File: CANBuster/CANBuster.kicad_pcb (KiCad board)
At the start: 2 copper layers, 100 x 100 mm, 182 parts, among them CON1 BARREL_JACK, J1 RJ45, J2 RJ45, J3 RJ12, P1 CONN_01X10, P10 CONN_02X04, P11 RS232-Programmer, P12 S88, P13 CONN_01X10, P14 CONN_01X10, P15 TRACK, P16 CONN_01X02, P17 USB_OTG, P18 CONN_01X04, P2 CONN_01X10, P3 CONN_01X03, P4 CONN_01X03, P5 CONN_01X03, P6 CONN_01X03, P7 CONN_01X02, P8 CONN_01X06, P9 CONN_01X04, Q1 BC547, Q2 BC547, SW1 SW_PUSH, SW2 SW_PUSH, U1 PIC18F45K80, U12 MCP2561, U2 MCP2561, U3 7805, U4 LTV-844, U5 LTV-844, U6 LTV-844, U7 LTV-844, U8 ISO1050, Y1 16MHz

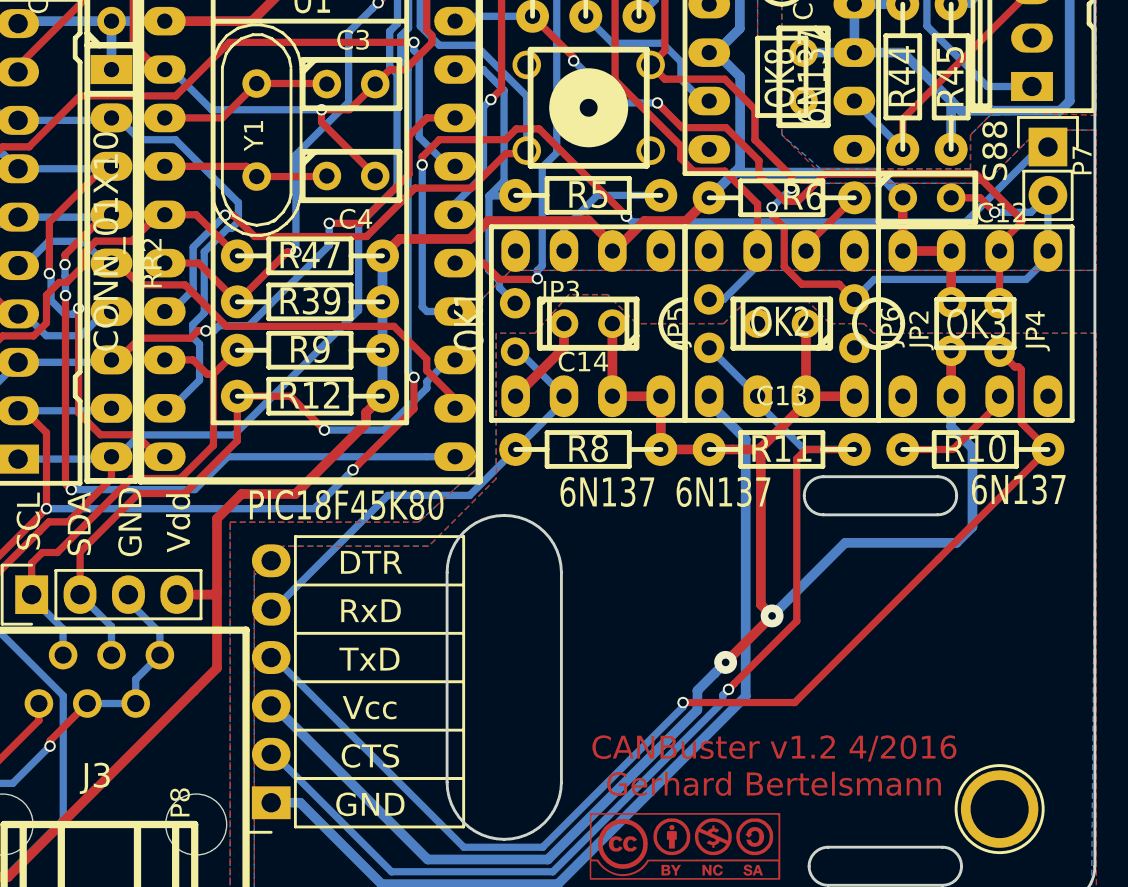
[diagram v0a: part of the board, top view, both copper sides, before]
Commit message: PCB: fix CCP2 pin
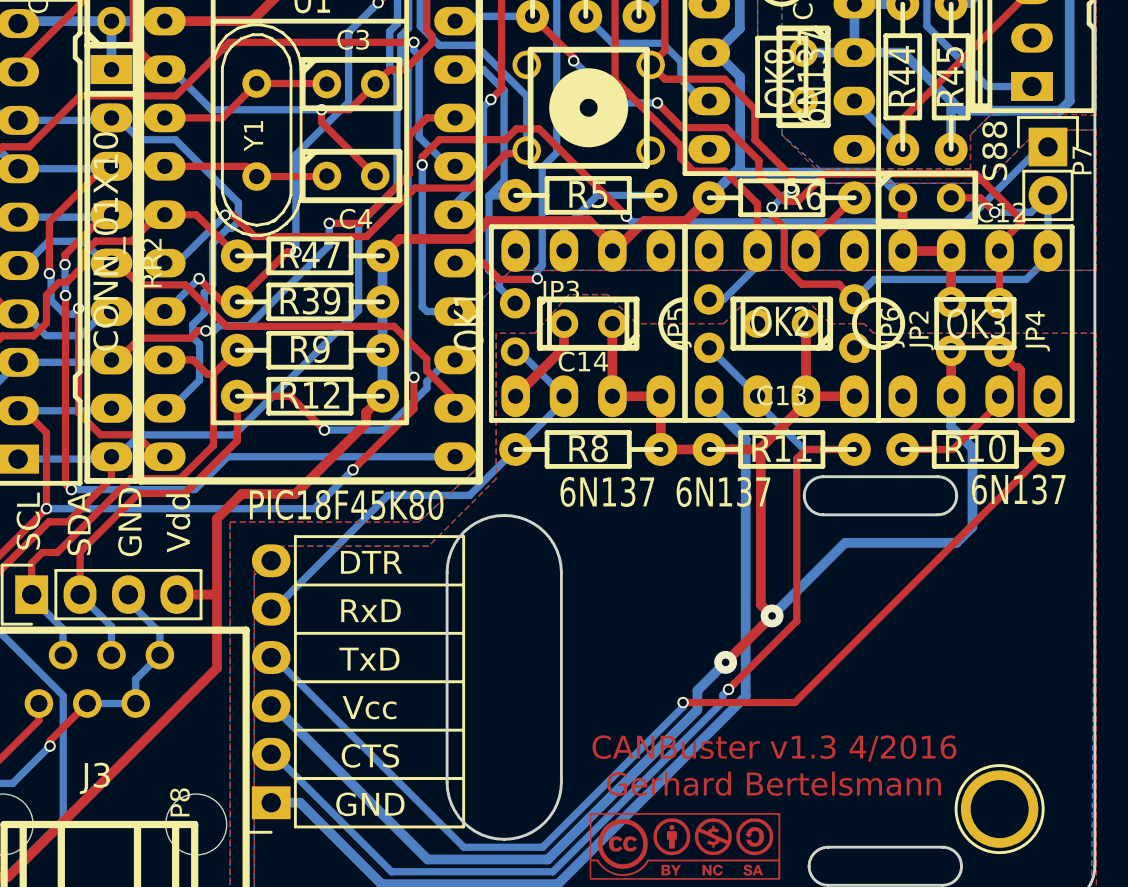
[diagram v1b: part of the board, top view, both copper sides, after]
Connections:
- U1 pad 16: /PWM1 -> /STATUS
- U1 pad 17: /STATUS -> /PWM1
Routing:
- net /STATUS: track 95.6 -> 93.3 mm
- net /PWM1: track 68.0 -> 68.4 mm, vias 2 -> 3
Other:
- board text added: "CANBuster v1.3 4/2016 Gerhard Bertelsmann"
- board text removed: "CANBuster v1.2 4/2016 Gerhard Bertelsmann"
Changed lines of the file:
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@@
-(kicad_pcb (version 4) (host pcbnew 4.0.1-stable)
+(kicad_pcb (version 4) (host pcbnew 4.0.2-4+6225~38~ubuntu14.04.1-stable)
   (general
     (links 464)
     (no_connects 0)
-    (area 70.028999 35.052999 170.179001 135.203001)
+    (area 69.215499 29.4545 181.99 144.85554)
     (thickness 1.6)
     (drawings 39)
-    (tracks 1769)
+    (tracks 1776)
     (zones 0)
     (modules 182)
@@
       (net 77 /SNIFF))
     (pad 16 thru_hole oval (at 13.97 7.62 270) (size 1.50114 2.19964) (drill 0.8001) (layers *.Cu *.Mask F.SilkS)
-      (net 26 /PWM1))
-    (pad 17 thru_hole oval (at 16.51 7.62 270) (size 1.50114 2.19964) (drill 0.8001) (layers *.Cu *.Mask F.SilkS)
       (net 59 /STATUS))
+    (pad 17 thru_hole oval (at 16.51 7.62 270) (size 1.50114 2.19964) (drill 0.8001) (layers *.Cu *.Mask F.SilkS)
+      (net 26 /PWM1))
     (pad 18 thru_hole oval (at 19.05 7.62 270) (size 1.50114 2.19964) (drill 0.8001) (layers *.Cu *.Mask F.SilkS)
       (net 30 /SCL))
@@
     (effects (font (size 1.2 1.2) (thickness 0.2)))
   )
-  (gr_text "CANBuster v1.2 4/2016\nGerhard Bertelsmann" (at 153.289 127.889) (layer F.Cu)
+  (gr_text "CANBuster v1.3 4/2016\nGerhard Bertelsmann" (at 153.289 127.889) (layer F.Cu)
     (effects (font (size 1.2 1.2) (thickness 0.25)))
   )
@@
   (segment (start 112.2172 86.233) (end 113.5888 86.233) (width 0.381) (layer B.Cu) (net 17))
   (segment (start 111.5822 85.598) (end 112.2172 86.233) (width 0.381) (layer B.Cu) (net 17))
-  (segment (start 121.63425 109.093) (end 121.285 109.093) (width 0.381) (layer B.Cu) (net 18))
-  (segment (start 125.150502 99.289842) (end 124.791442 99.648902) (width 0.381) (layer B.Cu) (net 18))
-  (segment (start 124.791442 99.648902) (end 124.59117 99.648902) (width 0.381) (layer B.Cu) (net 18))
-  (segment (start 124.59117 99.648902) (end 123.356341 100.883731) (width 0.381) (layer B.Cu) (net 18))
+  (segment (start 123.356341 103.008459) (end 123.407141 103.008459) (width 0.381) (layer B.Cu) (net 18))
   (segment (start 122.753498 105.360442) (end 123.112558 105.719502) (width 0.381) (layer B.Cu) (net 18))
   (segment (start 123.112558 105.719502) (end 123.112558 107.614692) (width 0.381) (layer B.Cu) (net 18))
-  (segment (start 123.356341 100.883731) (end 123.356341 104.094715) (width 0.381) (layer B.Cu) (net 18))
   (segment (start 123.356341 104.094715) (end 122.753498 104.697558) (width 0.381) (layer B.Cu) (net 18))
   (segment (start 122.753498 104.697558) (end 122.753498 105.360442) (width 0.381) (layer B.Cu) (net 18))
-  (segment (start 118.491 93.853) (end 118.82882 93.853) (width 0.381) (layer B.Cu) (net 18))
-  (segment (start 118.82882 93.853) (end 119.97182 94.996) (width 0.381) (layer B.Cu) (net 18))
+  (segment (start 121.63425 109.093) (end 123.112558 107.614692) (width 0.381) (layer B.Cu) (net 18))
+  (segment (start 123.356341 104.094715) (end 123.356341 103.008459) (width 0.381) (layer B.Cu) (net 18))
+  (segment (start 124.591164 99.648896) (end 124.591164 99.648902) (width 0.381) (layer B.Cu) (net 18))
+  (segment (start 123.7996 100.44046) (end 124.591164 99.648896) (width 0.381) (layer B.Cu) (net 18))
+  (segment (start 123.7996 102.616) (end 123.7996 100.44046) (width 0.381) (layer B.Cu) (net 18))
+  (segment (start 123.407141 103.008459) (end 123.7996 102.616) (width 0.381) (layer B.Cu) (net 18))
+  (segment (start 125.150502 98.295522) (end 125.150502 99.289842) (width 0.381) (layer B.Cu) (net 18))
+  (segment (start 125.150502 99.289842) (end 124.791442 99.648902) (width 0.381) (layer B.Cu) (net 18))
+  (segment (start 124.791442 99.648902) (end 124.591164 99.648902) (width 0.381) (layer B.Cu) (net 18))
+  (segment (start 119.97182 94.996) (end 118.82882 93.853) (width 0.381) (layer B.Cu) (net 18))
   (segment (start 119.97182 94.996) (end 121.85098 94.996) (width 0.381) (layer B.Cu) (net 18))
   (segment (start 121.85098 94.996) (end 125.150502 98.295522) (width 0.381) (layer B.Cu) (net 18))
-  (segment (start 125.150502 98.295522) (end 125.150502 99.289842) (width 0.381) (layer B.Cu) (net 18))
-  (segment (start 123.112558 107.614692) (end 121.63425 109.093) (width 0.381) (layer B.Cu) (net 18))
+  (segment (start 124.591164 99.648902) (end 124.59117 99.648902) (width 0.381) (layer B.Cu) (net 18))
+  (segment (start 121.63425 109.093) (end 121.285 109.093) (width 0.381) (layer B.Cu) (net 18))
+  (segment (start 118.491 93.853) (end 118.82882 93.853) (width 0.381) (layer B.Cu) (net 18))
   (segment (start 113.5888 93.98) (end 118.364 93.98) (width 0.381) (layer B.Cu) (net 18))
   (segment (start 118.364 93.98) (end 118.491 93.853) (width 0.381) (layer B.Cu) (net 18))
@@
   (segment (start 113.5888 111.76) (end 118.364 111.76) (width 0.381) (layer B.Cu) (net 25))
   (segment (start 118.364 111.76) (end 118.491 111.633) (width 0.381) (layer B.Cu) (net 25))
+  (segment (start 121.285 104.013) (end 121.3612 104.013) (width 0.381) (layer B.Cu) (net 26))
+  (segment (start 121.3612 104.013) (end 123.0884 102.2858) (width 0.381) (layer B.Cu) (net 26))
+  (via (at 123.0884 102.2858) (size 0.6) (drill 0.4) (layers F.Cu B.Cu) (net 26))
+  (segment (start 123.0884 102.2858) (end 124.3076 103.505) (width 0.381) (layer F.Cu) (net 26))
+  (segment (start 124.3076 103.505) (end 125.095 103.505) (width 0.381) (layer F.Cu) (net 26))
   (segment (start 160.602119 65.590401) (end 161.002999 65.590401) (width 0.381) (layer F.Cu) (net 26))
   (segment (start 161.002999 65.590401) (end 162.9156 63.6778) (width 0.381) (layer F.Cu) (net 26))
@@
   (via (at 128.1684 100.8888) (size 0.6) (drill 0.4) (layers F.Cu B.Cu) (net 26))
   (segment (start 127.7112 100.8888) (end 128.1684 100.8888) (width 0.381) (layer F.Cu) (net 26))
-  (segment (start 125.095 103.505) (end 123.063 101.473) (width 0.381) (layer F.Cu) (net 26))
-  (segment (start 123.063 101.473) (end 121.285 101.473) (width 0.381) (layer F.Cu) (net 26))
   (segment (start 151.0897 65.81967) (end 151.718655 65.190715) (width 0.381) (layer F.Cu) (net 27))
   (segment (start 162.9156 57.4548) (end 162.9156 57.3024) (width 0.381) (layer F.Cu) (net 27))
@@
   (segment (start 112.903 54.102) (end 115.951 54.102) (width 1.524) (layer B.Cu) (net 58))
   (segment (start 115.951 54.102) (end 117.348 52.705) (width 1.524) (layer B.Cu) (net 58))
+  (segment (start 121.285 101.473) (end 121.9454 101.473) (width 0.381) (layer B.Cu) (net 59))
+  (segment (start 121.9454 101.473) (end 122.77533 100.64307) (width 0.381) (layer B.Cu) (net 59))
   (segment (start 132.588 63.881) (end 131.206978 63.881) (width 0.381) (layer B.Cu) (net 59))
   (via (at 131.206978 63.881) (size 0.6) (drill 0.4) (layers F.Cu B.Cu) (net 59))
@@
   (segment (start 134.41685 97.53408) (end 137.3865 97.53408) (width 0.381) (layer F.Cu) (net 59))
   (segment (start 139.19814 95.72244) (end 140.2588 95.72244) (width 0.381) (layer F.Cu) (net 59))
-  (segment (start 121.285 104.013) (end 121.63425 104.013) (width 0.381) (layer B.Cu) (net 59))
   (via (at 124.46 98.9584) (size 0.6) (drill 0.4) (layers F.Cu B.Cu) (net 59))
-  (segment (start 121.63425 104.013) (end 122.77533 102.87192) (width 0.381) (layer B.Cu) (net 59))
-  (segment (start 122.77533 102.87192) (end 122.77533 100.64307) (width 0.381) (layer B.Cu) (net 59))
   (segment (start 122.77533 100.64307) (end 124.46 98.9584) (width 0.381) (layer B.Cu) (net 59))
   (segment (start 123.317 47.117) (end 124.192029 46.241971) (width 0.381) (layer F.Cu) (net 60))

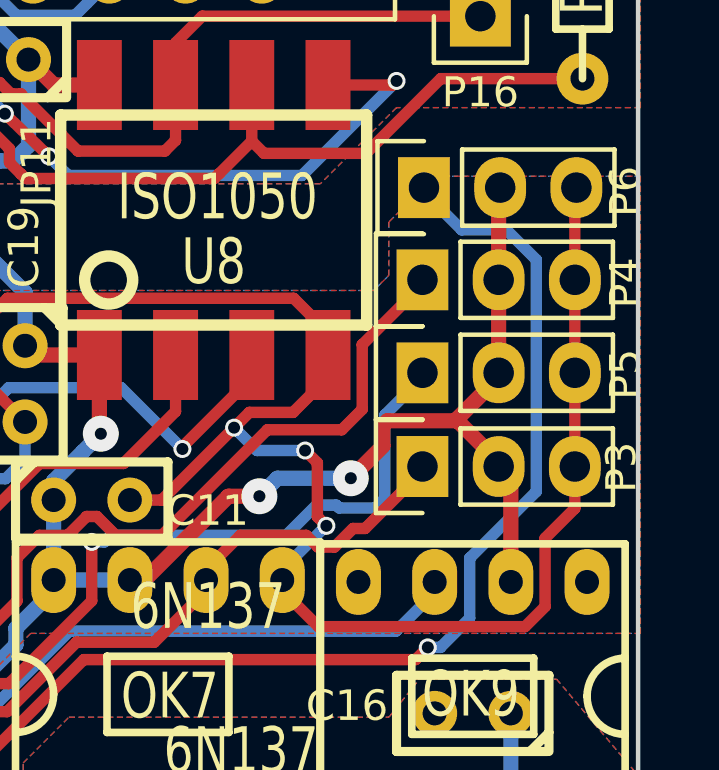
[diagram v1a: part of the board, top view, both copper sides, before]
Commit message: fix RC2 pin
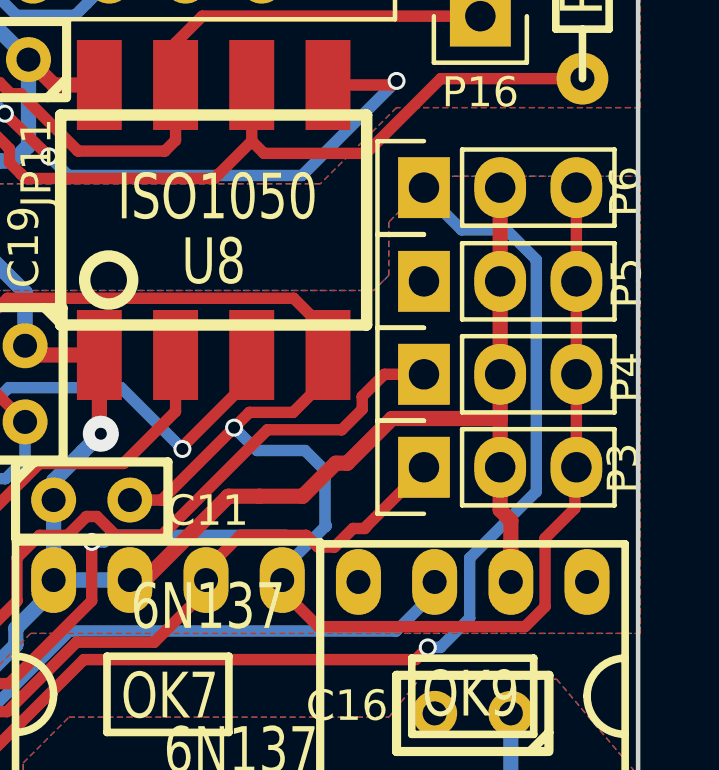
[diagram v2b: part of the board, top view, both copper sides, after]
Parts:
- moved P4 3.15 mm to (163.0, 60.5)
- moved P5 3.05 mm to (163.0, 57.4)
- moved P3 0.06 mm to (163.0, 63.6)
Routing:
- net /PWM3: track 57.9 -> 49.4 mm
- net /PWM2: track 65.5 -> 63.2 mm
- net VDD: track 337.5 -> 337.6 mm, vias 10 -> 8
- net GND: track 258.0 -> 258.1 mm, vias 11 -> 9

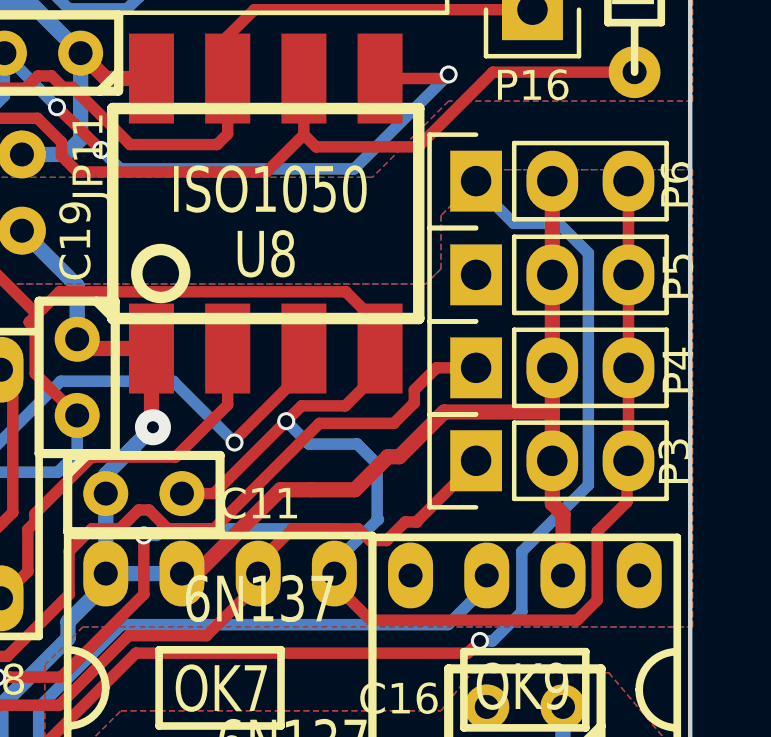
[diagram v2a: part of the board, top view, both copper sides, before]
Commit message: fix PCB routing
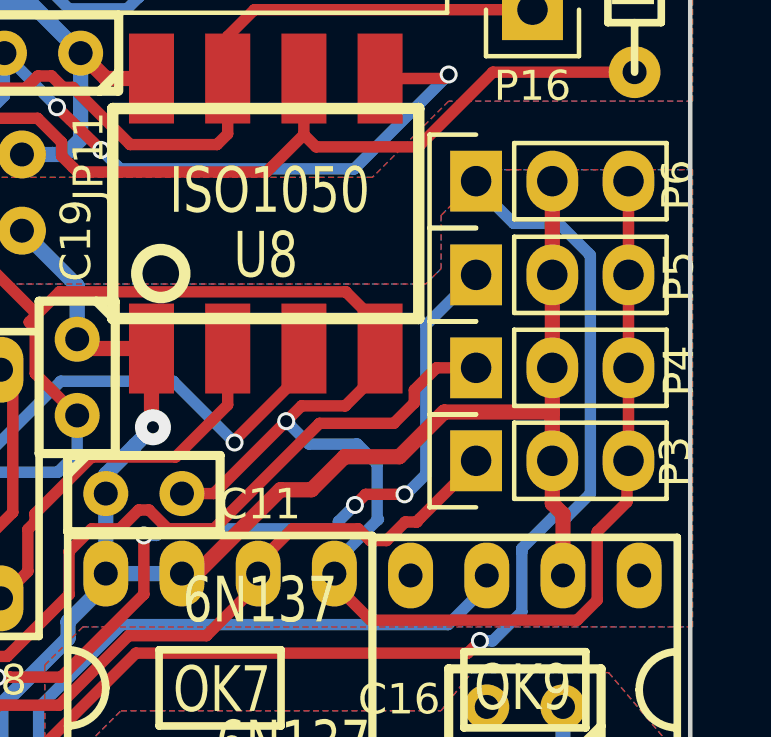
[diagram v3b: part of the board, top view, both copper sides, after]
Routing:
- net /PWM3: track 49.4 -> 60.5 mm, vias 6 -> 8

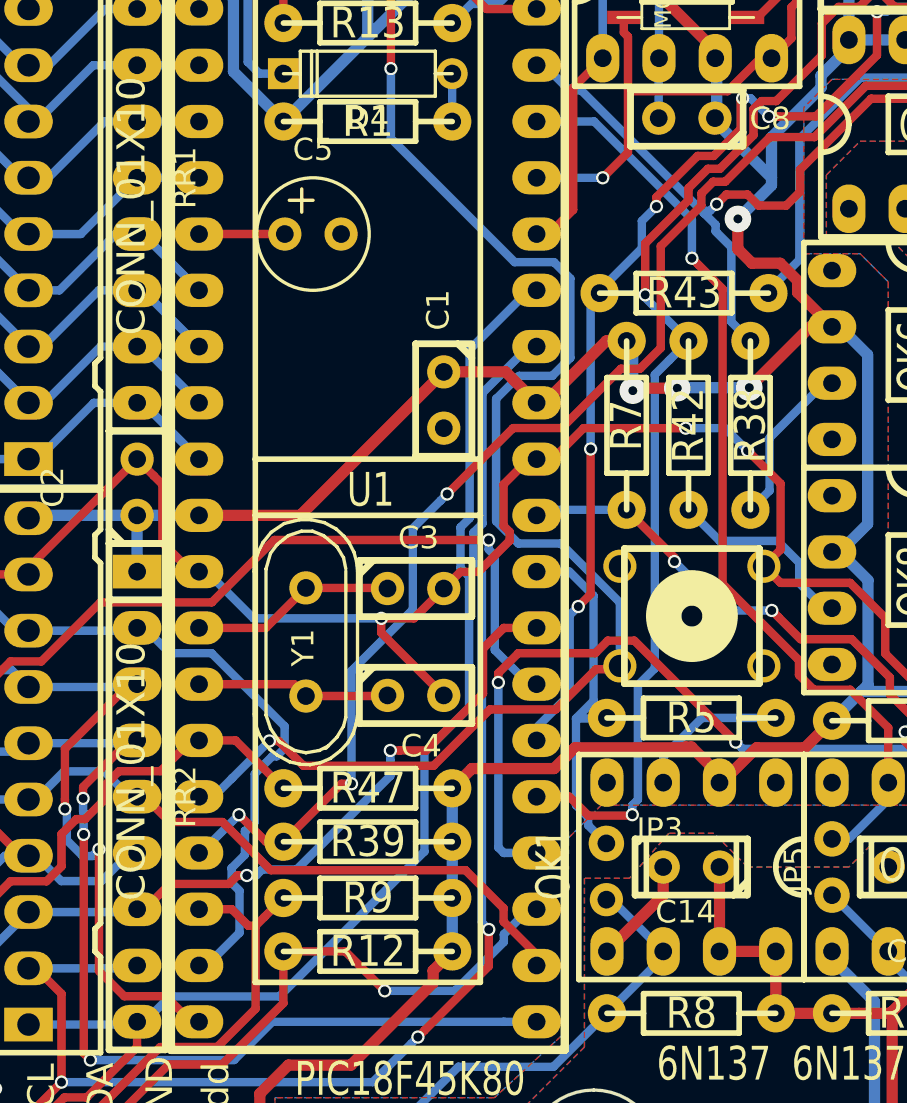
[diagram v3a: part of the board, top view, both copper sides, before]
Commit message: optimize PCB routing - avoid some vias
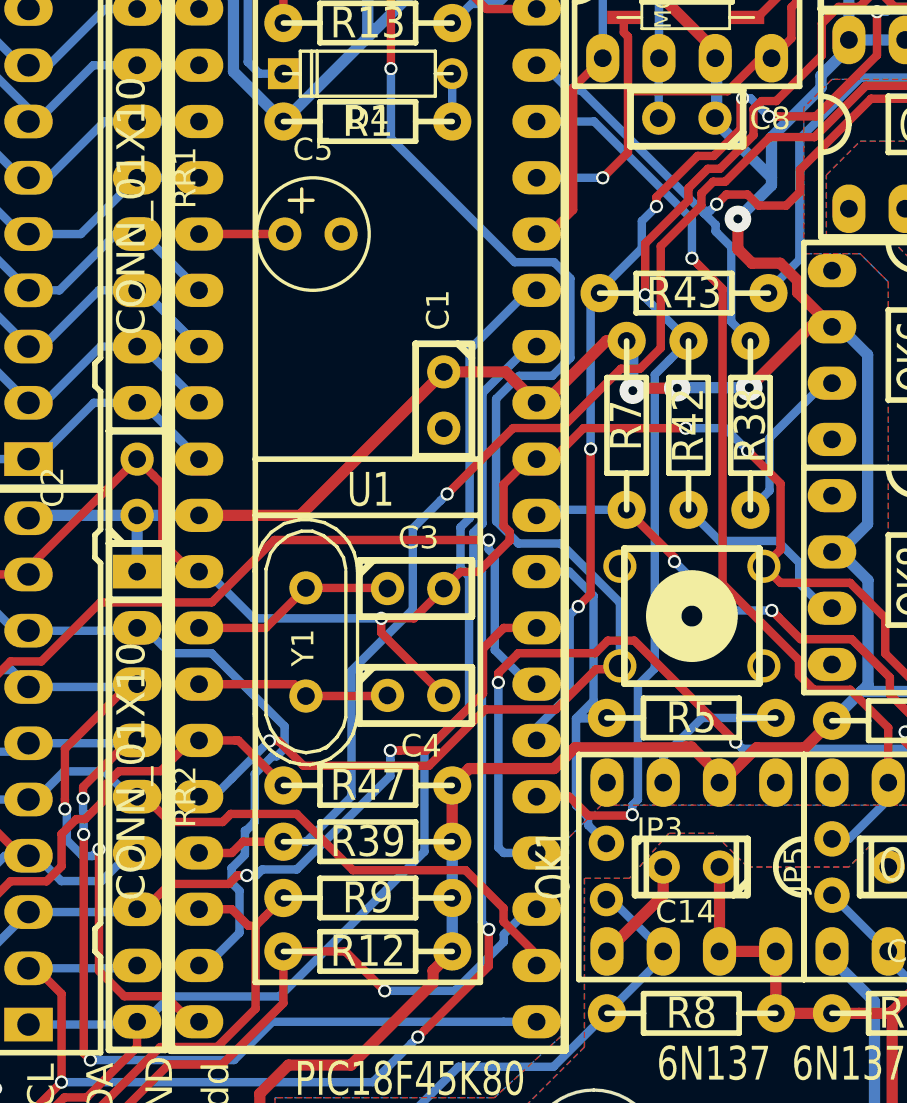
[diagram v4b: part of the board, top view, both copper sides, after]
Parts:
- moved R47 0.13 mm to (128.9, 101.0)
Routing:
- net /PWM1: track 68.5 -> 67.9 mm, vias 3 -> 1
